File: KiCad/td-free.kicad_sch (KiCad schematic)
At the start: 6 parts, among them J1 Conn_01x02_Pin, Q1 2N7002, U1 ESP32-C3_SUPERMINI, U2 VEML7700-TT

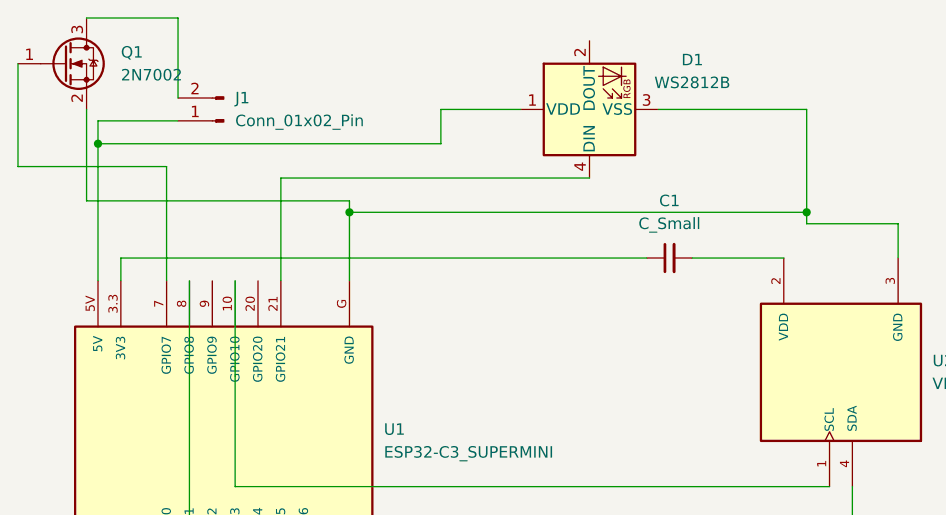
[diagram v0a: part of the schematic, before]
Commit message: Add V1.2 PCB without wrong condensator
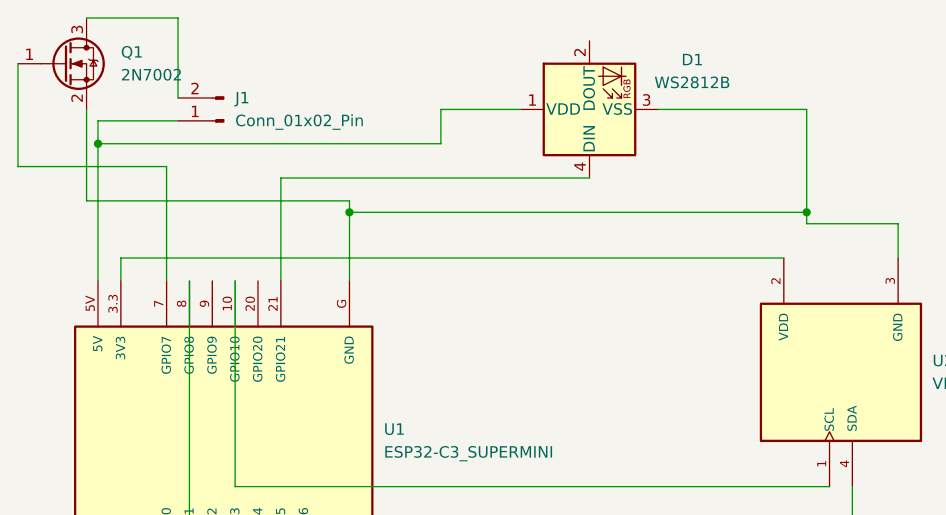
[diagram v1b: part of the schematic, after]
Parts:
- removed C1: C_Small, Capacitor_SMD:C_0603_1608Metric_Pad1.08x0.95mm_HandSolder, symbol Device:C_Small
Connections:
- net at U1.3.3 (3V3): now also U2.2 (VDD)
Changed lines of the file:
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@@
 	(wire
 		(pts
-			(xy 101.6 59.69) (xy 111.76 59.69)
-		)
-		(stroke
-			(width 0)
-			(type default)
-		)
-	)
-	(wire
-		(pts
-			(xy 38.1 59.69) (xy 96.52 59.69)
+			(xy 38.1 59.69) (xy 111.76 59.69)
 		)
 		(stroke
@@
 		)
 	)
-	(symbol
-		(lib_id "Device:C_Small")
-		(at 99.06 59.69 90)
-		(unit 1)
-		(exclude_from_sim no)
-		(in_bom yes)
-		(on_board yes)
-		(dnp no)
-		(fields_autoplaced yes)
-		(property "Reference" "C1"
-			(at 99.0663 53.34 90)
-			(effects
-				(font
-					(size 1.27 1.27)
-				)
-			)
-		)
-		(property "Value" "C_Small"
-			(at 99.0663 55.88 90)
-			(effects
-				(font
-					(size 1.27 1.27)
-				)
-			)
-		)
-		(property "Footprint" "Capacitor_SMD:C_0603_1608Metric_Pad1.08x0.95mm_HandSolder"
-			(at 99.06 59.69 0)
-			(effects
-				(font
-					(size 1.27 1.27)
-				)
-				(hide yes)
-			)
-		)
-		(property "Datasheet" "~"
-			(at 99.06 59.69 0)
-			(effects
-				(font
-					(size 1.27 1.27)
-				)
-				(hide yes)
-			)
-		)
-		(property "Description" "Unpolarized capacitor, small symbol"
-			(at 99.06 59.69 0)
-			(effects
-				(font
-					(size 1.27 1.27)
-				)
-				(hide yes)
-			)
-		)
-		(pin "1"
-		)
-		(pin "2"
-		)
-		(instances
-			(project ""
-				(path "/029a7aea-43c9-4f1d-af51-7a1360dad1ba"
-					(reference "C1")
-					(unit 1)
-				)
-			)
-		)
-	)

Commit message: :sparkles: First Prototype for improved PCB
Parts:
- removed U1: ESP32-C3_SUPERMINI, ESP32-C3_SUPERMINI:MODULE_ESP32-C3_SUPERMINI, symbol ESP32-C3_SUPERMINI:ESP32-C3_SUPERMINI
- added C1, C4, C6: 10uF, Capacitor_SMD:C_0805_2012Metric_Pad1.18x1.45mm_HandSolder, symbol Device:C_Small
- added C2, C3: 22uF, Capacitor_SMD:C_0805_2012Metric_Pad1.18x1.45mm_HandSolder, symbol Device:C_Small
- added C5: 0.1uF, Capacitor_SMD:C_0805_2012Metric_Pad1.18x1.45mm_HandSolder, symbol Device:C_Small
- added D2: SMAJ5.0A, Diode_SMD:D_SMA, symbol Diode:SMAJ5.0A
- added J2: USB_C_Receptacle_USB2.0_14P, Connector_USB:USB_C_Receptacle_GCT_USB4105-xx-A_16P_TopMnt_Horizontal, symbol Connector:USB_C_Receptacle_USB2.0_14P
- added R1, R2: 5k1, Resistor_SMD:R_0805_2012Metric_Pad1.20x1.40mm_HandSolder, symbol Device:R_Small
- added R3: 10kO, Resistor_SMD:R_0805_2012Metric_Pad1.20x1.40mm_HandSolder, symbol Device:R_Small
- added U1: ESP32-C3-WROOM-02, PCM_Espressif:ESP32-C3-WROOM-02, symbol PCM_Espressif:ESP32-C3-WROOM-02
- added U3: AMS1117-3.3, Package_TO_SOT_SMD:SOT-223-3_TabPin2, symbol Regulator_Linear:AMS1117-3.3
- added U4: VEML3328, footprints:SMD_L3328_VIS, symbol 2025-03-01_22-07-39:VEML3328
- added U5: TPD4E05U06DQA, Package_SON:USON-10_2.5x1.0mm_P0.5mm, symbol Power_Protection:TPD4E05U06DQA
- J1: footprint Connector_PinHeader_2.00mm:PinHeader_1x02_P2.00mm_Horizontal -> Connector_PinHeader_2.54mm:PinHeader_1x02_P2.54mm_Vertical
- U2: footprint VEML7700-TT:XDCR_VEML7700-TT -> VEML7700_TR:XDCR_VEML7700-TR; symbol VEML7700-TT:VEML7700-TT -> VEML7700-TR:VEML7700-TR; MAXIMUM_PACKAGE_HEIGHT 2.35 mm -> 3 mm; SNAPEDA_PN VEML7700-TT -> VEML7700-TR
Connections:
- net LED_C: now reaches Q1.1 (G)
- net LED_C: now also U1.6 (GPIO7)
- net GND: now reaches D1.3 (VSS), Q1.2 (S), U2.3 (GND)
- net GND: now also C1.2, C2.2, C3.1, C4.1, C5.1, C6.1, D2.2 (A2), J2.A1 (GND), J2.A12 (GND), J2.B1 (GND), J2.B12 (GND), J2.S1 (SHIELD), R1.2, R2.2, U1.19 (GND), U1.9 (GND), U3.1 (GND), U4.1 (GND), U5.3 (GND), U5.8 (GND)
- net SCL: now reaches U2.1 (SCL)
- net SCL: now also U1.10 (GPIO10), U4.3 (SCL)
- net RGB_DATA: now reaches D1.4 (DIN)
- net RGB_DATA: now also U1.8 (GPIO9)
- net +3V3: now reaches U2.2 (VDD)
- net +3V3: now also C2.1, C3.2, C4.2, C5.2, C6.2, R3.1, U1.1 (3V3), U3.2 (VO), U4.4 (VDD)
- net VBUS: now reaches D1.1 (VDD), J1.1 (Pin_1)
- net VBUS: now also C1.1, D2.1 (A1), J2.A4 (VBUS), J2.A9 (VBUS), J2.B4 (VBUS), J2.B9 (VBUS), U3.3 (VI)
- net SDA: now reaches U2.4 (SDA)
- net SDA: now also U1.7 (GPIO8), U4.2 (SDA)
- new net: J2.A5 (CC1), R1.1
- new net: R3.2, U1.2 (EN/CHIP_PU)
- new net: J2.B5 (CC2), R2.1
- new net USB_D+: J2.A6 (D+), J2.B6 (D+), U1.14 (GPIO19/USB_D+), U5.1 (D1+)
- new net USB_D-: J2.A7 (D-), J2.B7 (D-), U1.13 (GPIO18/USB_D-), U5.2 (D1-)
- no-connect marks 0 -> 16
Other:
- note added: "3V3 Regulator"
- note added: "USB + ESD Protection"
- moved on the sheet: D1, J1, Q1, U2

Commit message: :sparkles: First test with new PCB
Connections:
- net SCL2: now reaches U1.4 (GPIO5/ADC2_CH0)
- net SCL2: now also U2.1 (SCL)
- net SDA2: now reaches U1.5 (GPIO6)
- net SDA2: now also U2.4 (SDA)
- net SCL renamed SCL1
- net SCL1: no longer U2.1 (SCL)
- net SDA renamed SDA1
- net SDA1: no longer U2.4 (SDA)
- no-connect marks 16 -> 14
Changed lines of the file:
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@@
 	(title_block
 		(title "Td-Free")
-		(rev "0")
+		(rev "1")
 	)
 	(text "3V3 Regulator"
@@
 	)
 	(no_connect
-		(at 91.44 106.68)
-	)
-	(no_connect
 		(at 35.56 91.44)
 	)
@@
 	)
 	(no_connect
-		(at 91.44 109.22)
-	)
-	(no_connect
 		(at 91.44 83.82)
 	)
@@
 	(wire
 		(pts
+			(xy 91.44 106.68) (xy 96.52 106.68)
+		)
+		(stroke
+			(width 0)
+			(type default)
+		)
+	)
+	(wire
+		(pts
 			(xy 262.89 17.78) (xy 271.78 17.78)
 		)
@@
 		(pts
 			(xy 167.64 36.83) (xy 167.64 39.37)
+		)
+		(stroke
+			(width 0)
+			(type default)
+		)
+	)
+	(wire
+		(pts
+			(xy 91.44 109.22) (xy 96.52 109.22)
 		)
 		(stroke
@@
 		)
 	)
-	(label "SCL"
+	(label "SCL2"
 		(at 255.27 59.69 0)
 		(effects
@@
 		)
 	)
-	(label "SCL"
+	(label "SCL1"
 		(at 236.22 121.92 0)
 		(effects
@@
 		)
 	)
-	(label "SDA"
+	(label "SDA1"
 		(at 96.52 114.3 0)
 		(effects
@@
 		)
 	)
-	(label "SDA"
+	(label "SDA1"
 		(at 186.69 121.92 0)
 		(effects
@@
 		)
 	)
-	(label "SDA"
+	(label "SCL2"
+		(at 96.52 106.68 0)
+		(effects
+			(font
+				(size 1.27 1.27)
+			)
+			(justify left bottom)
+		)
+	)
+	(label "SDA2"
 		(at 257.81 57.15 0)
 		(effects
@@
 		)
 	)
+	(label "SDA2"
+		(at 96.52 109.22 0)
+		(effects
+			(font
+				(size 1.27 1.27)
+			)
+			(justify left bottom)
+		)
+	)
 	(label "USB_D-"
 		(at 96.52 91.44 0)
@@
 		)
 	)
-	(label "SCL"
+	(label "SCL1"
 		(at 96.52 119.38 0)
 		(effects

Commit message: :sparkles: PCB Progress
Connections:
- net RGB_DATA: now also U1.3 (GPIO4/ADC1_CH4); no longer U1.8 (GPIO9)
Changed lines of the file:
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@@
-	)
-	(no_connect
-		(at 91.44 104.14)
 	)
 	(no_connect
@@
 	)
 	(no_connect
+		(at 91.44 116.84)
+	)
+	(no_connect
 		(at 182.88 33.02)
 	)
@@
 	(wire
 		(pts
-			(xy 91.44 116.84) (xy 96.52 116.84)
-		)
-		(stroke
-			(width 0)
-			(type default)
-		)
-	)
-	(wire
-		(pts
 			(xy 185.42 20.32) (xy 200.66 20.32)
 		)
@@
 	(wire
 		(pts
+			(xy 91.44 104.14) (xy 96.52 104.14)
+		)
+		(stroke
+			(width 0)
+			(type default)
+		)
+	)
+	(wire
+		(pts
 			(xy 91.44 106.68) (xy 96.52 106.68)
 		)
@@
 			(width 0)
 			(type default)
+		)
+	)
+	(label "RGB_DATA"
+		(at 96.52 104.14 0)
+		(effects
+			(font
+				(size 1.27 1.27)
+			)
+			(justify left bottom)
 		)
 	)
@@
 		(effects
 			(font
-				(size 1.27 1.27)
-			)
-			(justify left bottom)
-		)
-	)
-	(label "RGB_DATA"
-		(at 96.52 116.84 0)
-		(effects
-			(font

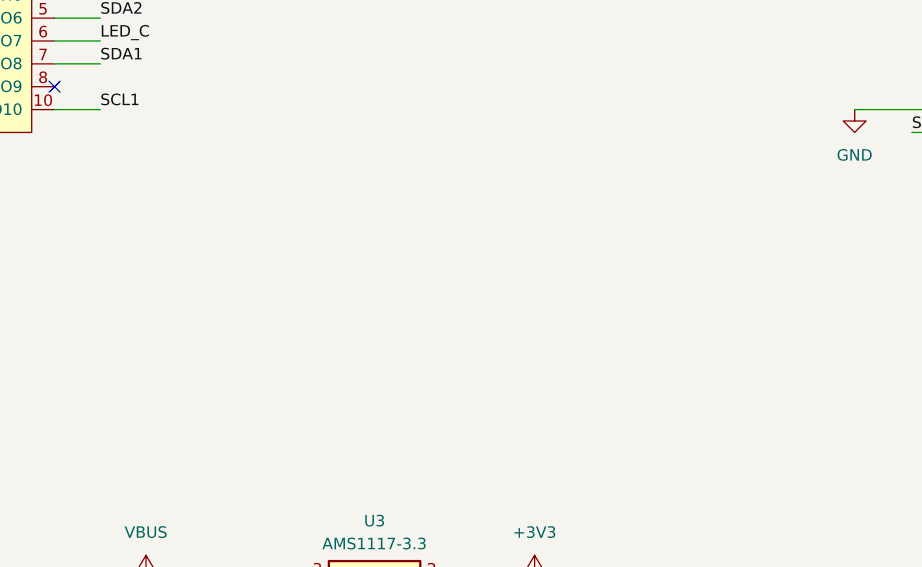
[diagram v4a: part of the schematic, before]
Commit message: :sparkles: New PCB working, software backwards compatible
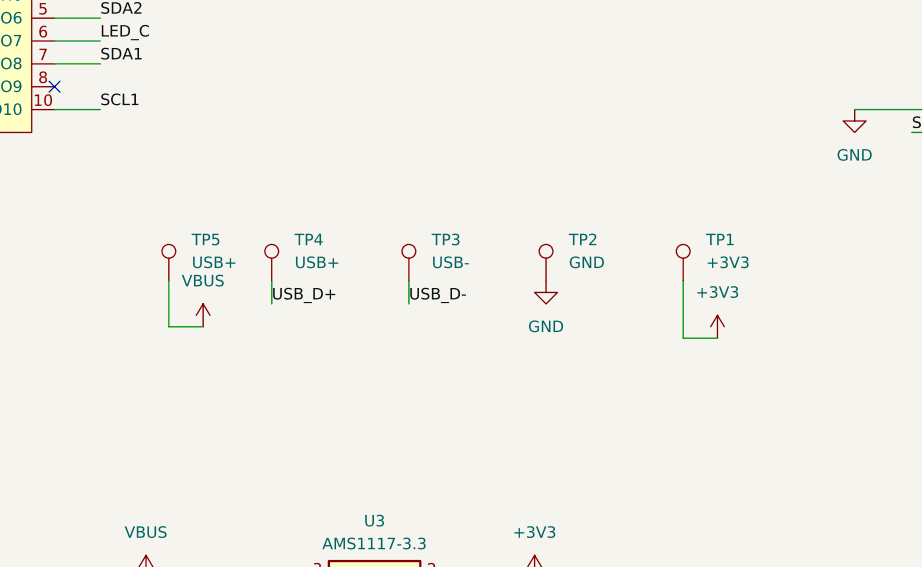
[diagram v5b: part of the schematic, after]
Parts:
- added TP1: +3V3, TestPoint:TestPoint_Pad_D1.0mm, symbol Connector:TestPoint
- added TP2: GND, TestPoint:TestPoint_Pad_D1.0mm, symbol Connector:TestPoint
- added TP3: USB-, TestPoint:TestPoint_Pad_D1.0mm, symbol Connector:TestPoint
- added TP4, TP5: USB+, TestPoint:TestPoint_Pad_D1.0mm, symbol Connector:TestPoint
- U2: footprint VEML7700_TR:XDCR_VEML7700-TR -> VEML7700_TR:XDCR_VEML7700-TT
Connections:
- net +3V3: now also TP1.1
- net GND: now also TP2.1
- net USB_D+: now also TP4.1
- net USB_D-: now also TP3.1
- net VBUS: now also TP5.1
